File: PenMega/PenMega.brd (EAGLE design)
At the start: 25.4 x 25.4 mm, 18 parts, among them IC2 REG1117, U1 ATMEGA328P_TQFP, U2 USD-SOCKET, Y1 16MHZ

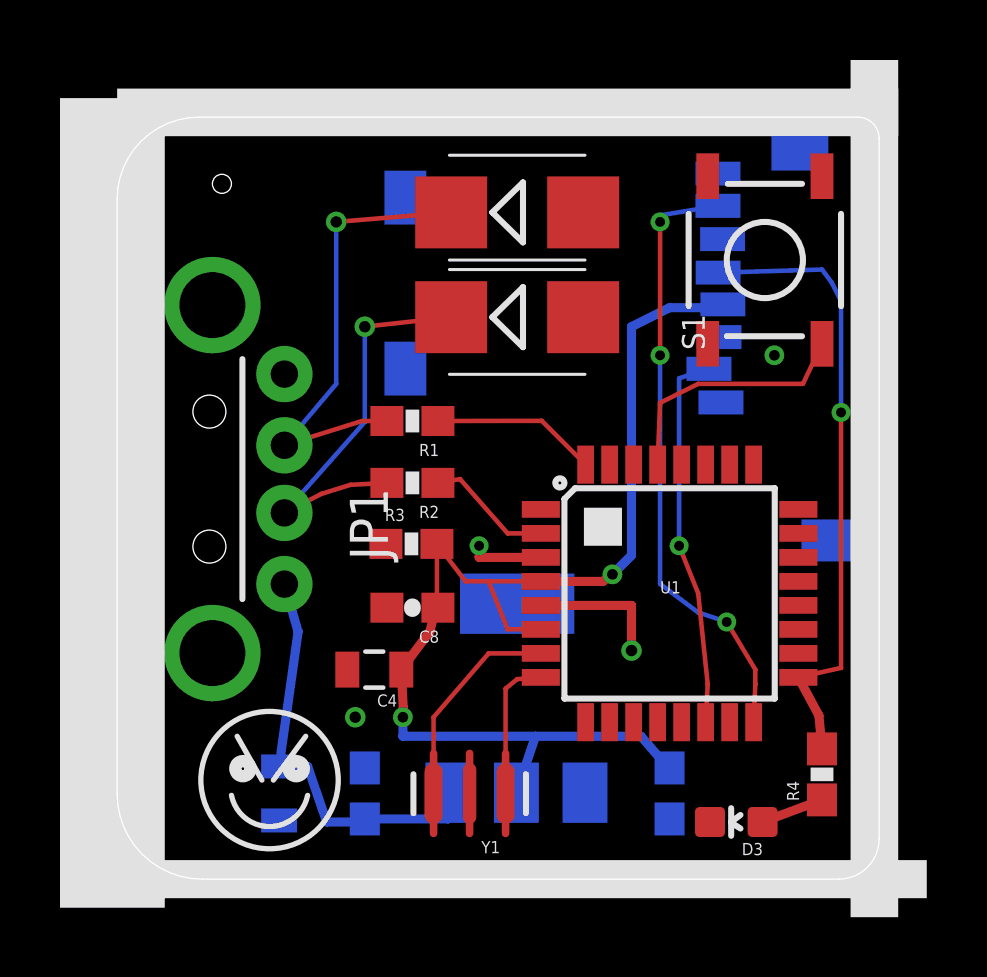
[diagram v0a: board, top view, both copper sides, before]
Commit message: Trying to make this work, as of now first sent to manufacturing did not work with 6mills paths. changed to 10 mills.
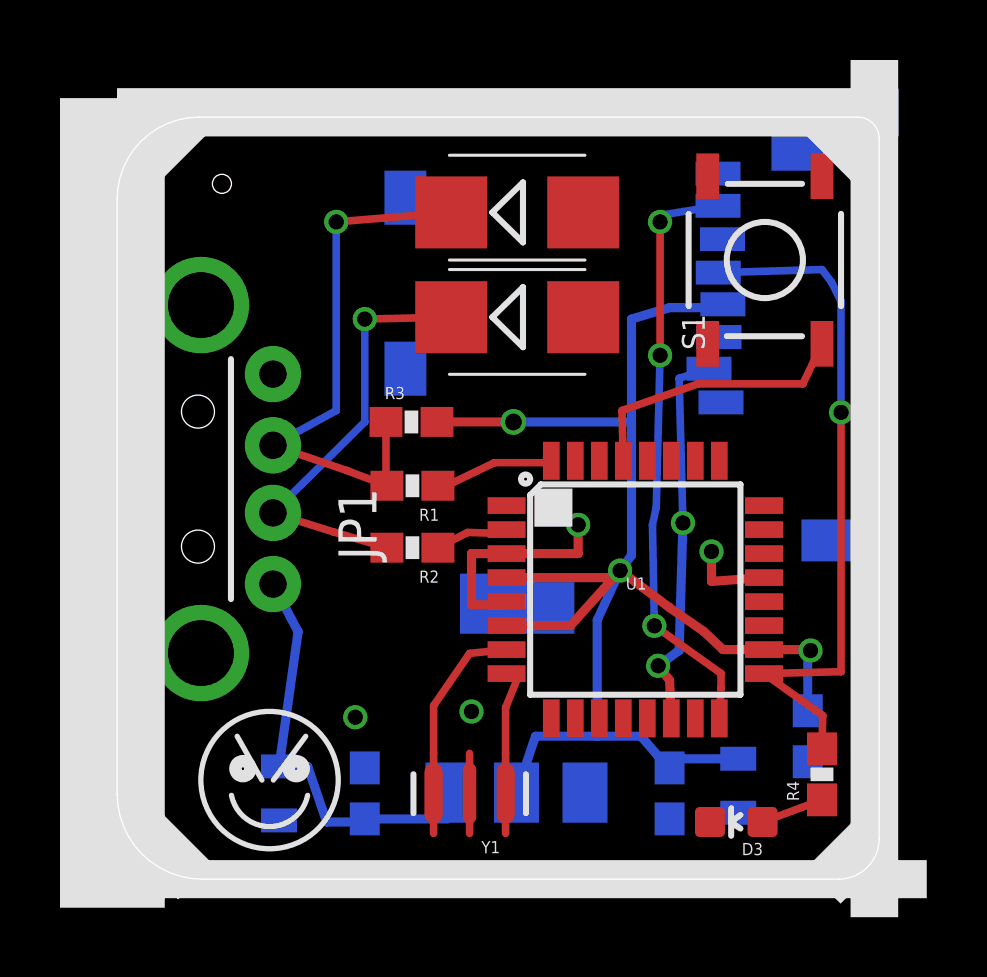
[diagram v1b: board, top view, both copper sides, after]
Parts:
- R3: value (none) -> 1.5k
- moved C8 13.9 mm to (23.0, 4.76), flipped to the bottom, turned to 270 degrees
- moved C4 12.7 mm to (20.7, 3.11), flipped to the bottom, turned to 270 degrees
- moved R3 4.06 mm to (9.81, 15.2)
- moved R1 2.16 mm to (9.84, 13.1)
- moved R2 2.16 mm to (9.84, 11.0)
- moved U1 1.15 mm to (17.3, 9.65)
- moved JP1 0.38 mm to (2.79, 13.3)
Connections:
- net N$3 renamed D+
- net N$4 renamed D-
- net GND: now also U1.21
- net VCC: now also U1.18
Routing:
- net VCC: track 39.5 -> 51.4 mm, vias 2 -> 3
- net D+: track 15.5 -> 18.7 mm
- net GND: track 7.04 -> 10.3 mm
- net SCK: track 20.9 -> 23.1 mm
- net N$5: track 4.26 -> 2.44 mm
- net N$6: track 5.53 -> 3.95 mm
- net N$7: track 8.45 -> 9.34 mm
- net D-: track 13.7 -> 14.6 mm
- net N$2: track 5.76 -> 4.94 mm
- net MISO: track 20.4 -> 19.9 mm
- net SDCS: track 12.6 -> 12.9 mm, vias 1 -> 2
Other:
- board text added: "V0.2"
- board text removed: "V0.1"

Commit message: Partial fix for penmega. Removed un needed zener diodes
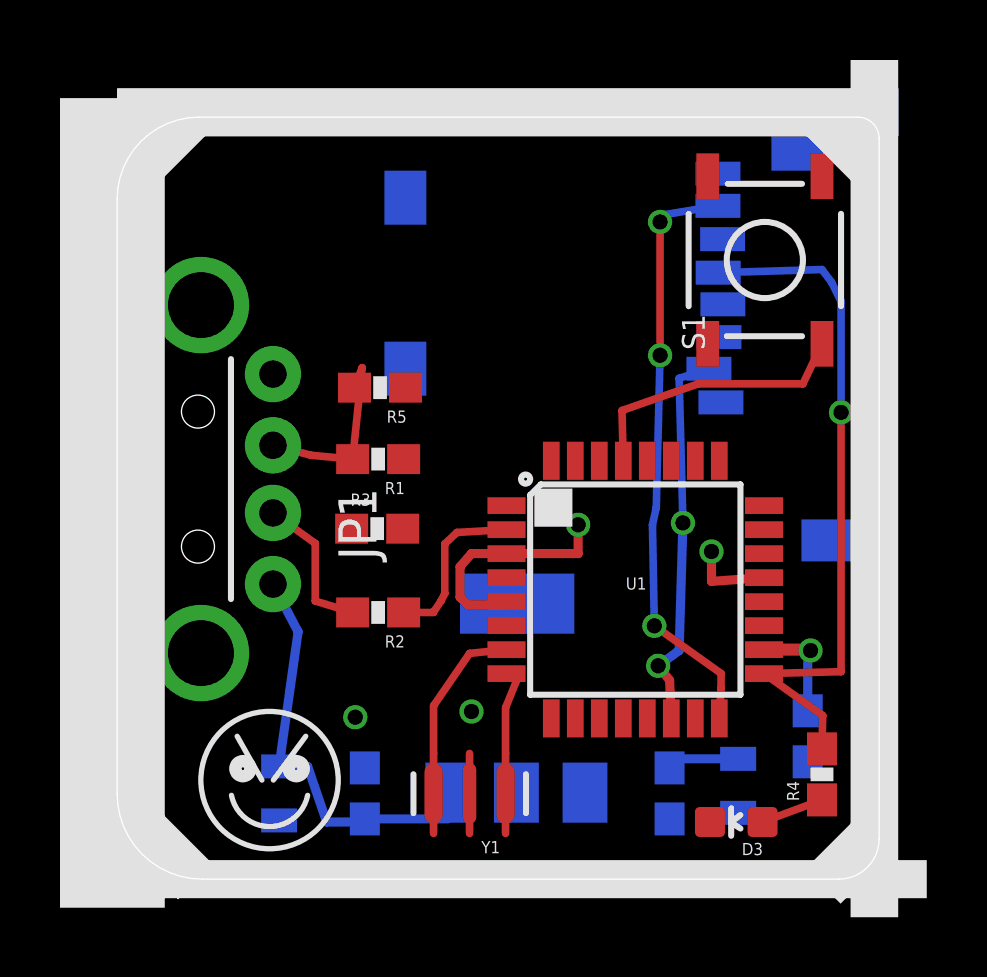
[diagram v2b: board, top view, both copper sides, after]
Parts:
- removed D1, D2: (no value), digital-ic:SMB
- added R5: 1M, SparkFun-Passives:0603-RES
- C8: value 22p -> 100n
- moved R3 3.74 mm to (8.67, 11.7)
- moved R2 2.44 mm to (8.70, 8.89)
- moved R1 1.45 mm to (8.70, 14.0)
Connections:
- removed net D+: D1.C, JP1.D+, R1.2, R3.1
- new net N$3: JP1.D+, R1.2, R5.2
- net D-: now also R3.1; no longer D2.C
- net GND: now also R5.1; no longer D1.A, D2.A
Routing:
- net VCC: track 51.4 -> 6.27 mm, vias 3 -> 1
- net D+: track 18.7 -> 0.00 mm, vias 1 -> 0
- net D-: track 14.6 -> 4.96 mm, vias 1 -> 0
- net N$3: track 0.00 -> 6.48 mm
- net N$6: track 3.95 -> 0.00 mm
- net N$5: track 2.44 -> 5.85 mm

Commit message: Partially working on fixing PenMega. Work in progress
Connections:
- net GND: now also U2.CD1, U2.CD2
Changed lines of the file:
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@@
 <contactref element="C8" pad="2"/>
 <contactref element="R5" pad="1"/>
+<contactref element="U2" pad="CD1"/>
+<contactref element="U2" pad="CD2"/>
 <wire x1="20.180653125" y1="21.33414375" x2="22.7575" y2="24.315" width="0" layer="19" extent="16-16"/>
 <wire x1="19.685" y1="17.8435" x2="20.180653125" y2="21.33414375" width="0" layer="19" extent="1-16"/>
@@
 <wire x1="23.7575" y1="11.292" x2="21.5646" y2="10.052" width="0" layer="19" extent="1-16"/>
 <wire x1="15.367" y1="10.852" x2="19.812" y2="10.922" width="0" layer="19" extent="1-1"/>
-<wire x1="9.613" y1="16.383" x2="11.43" y2="10.414" width="0" layer="19" extent="1-1"/>
 <wire x1="11.811" y1="5.588" x2="11.684" y2="9.144" width="0" layer="19" extent="1-1"/>
 <wire x1="11.7475" y1="4.191" x2="11.811" y2="5.588" width="0" layer="19" extent="1-1"/>
@@
 <wire x1="20.701" y1="2.2115" x2="19.7605" y2="1.905" width="0" layer="19" extent="1-16"/>
 <wire x1="23.01875" y1="3.9125" x2="20.701" y2="2.2115" width="0" layer="19" extent="16-16"/>
-<wire x1="5.194" y1="16.835" x2="9.613" y2="16.383" width="0" layer="19" extent="1-1"/>
+<wire x1="9.613" y1="16.383" x2="11.811" y2="10.852" width="0" layer="19" extent="1-1"/>
+<wire x1="9.6075" y1="17.015" x2="9.613" y2="16.383" width="0" layer="19" extent="1-16"/>
+<wire x1="5.194" y1="16.835" x2="9.6075" y2="17.015" width="0" layer="19" extent="16-16"/>
+<wire x1="9.6075" y1="22.715" x2="9.6075" y2="17.015" width="0" layer="19" extent="16-16"/>
 </signal>
 <signal name="N$12">
